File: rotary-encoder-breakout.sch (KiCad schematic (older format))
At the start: 3 parts, among them P4 CONN_01X02, P5 CONN_01X03

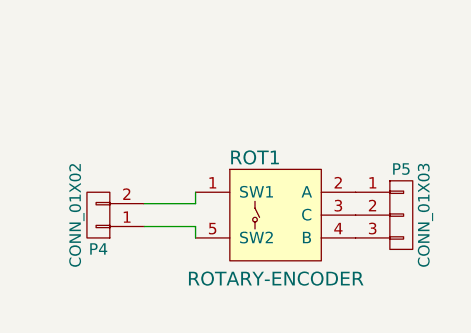
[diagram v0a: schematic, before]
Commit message: create version with pull-up resistors
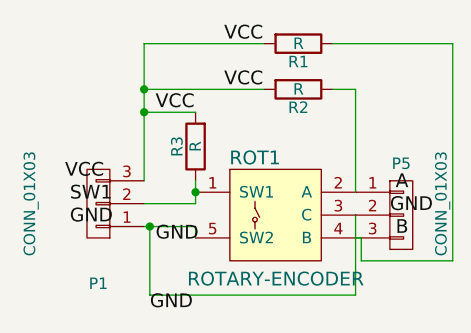
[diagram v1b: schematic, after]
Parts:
- removed P4: CONN_01X02, Pin_Headers:Pin_Header_Straight_1x02, symbol CONN_01X02
- added P1: CONN_01X03, Pin_Headers:Pin_Header_Straight_1x03, symbol CONN_01X03
- added R1, R2, R3: R, Resistors_SMD:R_1206, symbol R
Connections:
- net at P5.1 (P1), ROT1.2 (A): now also R2.1
- net at P5.2 (P2), ROT1.3 (C): now also ROT1.5 (SW2), P1.1 (P1)
- net at P5.3 (P3), ROT1.4 (B): now also R1.1
- net at ROT1.1 (SW1): now also P1.2 (P2), R3.1
- new net VCC: P1.3 (P3), R1.2, R2.2, R3.2
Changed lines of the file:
@@
 LIBS:Symbols_Transformer-Diskrete_RevA
 LIBS:sparkfun
+LIBS:rotary-encoder-breakout-cache
 EELAYER 25 0
 EELAYER END
@@
 U 1 1 587E787E
 P 3075 2225
-F 0 "P5" H 3075 2425 50  0000 C CNN
-F 1 "CONN_01X03" V 3175 2225 50  0000 C CNN
+F 0 "P5" H 3075 2450 50  0000 C CNN
+F 1 "CONN_01X03" V 3250 2275 50  0000 C CNN
 F 2 "Pin_Headers:Pin_Header_Straight_1x03" H 3075 2225 50  0001 C CNN
 F 3 "" H 3075 2225 50  0000 C CNN
@@
 	1    0    0    -1
 $EndComp
-$Comp
-L CONN_01X02 P4
-U 1 1 587E7945
-P 1750 2225
-F 0 "P4" H 1750 2375 50  0000 C CNN
-F 1 "CONN_01X02" V 1850 2225 50  0000 C CNN
-F 2 "Pin_Headers:Pin_Header_Straight_1x02" H 1750 2225 50  0001 C CNN
-F 3 "" H 1750 2225 50  0000 C CNN
-	1    1750 2225
-	-1   0    0    1
-$EndComp
-Wire Wire Line
-	1950 2175 2175 2175
-Wire Wire Line
-	2175 2175 2175 2125
-Wire Wire Line
-	1950 2275 2175 2275
-Wire Wire Line
-	2175 2275 2175 2325
 $Comp
 L ROTARY-ENCODER ROT1
@@
 	1    0    0    -1
 $EndComp
+$Comp
+L R R1
+U 1 1 58C20278
+P 2625 1475
+F 0 "R1" V 2705 1475 50  0000 C CNN
+F 1 "R" V 2625 1475 50  0000 C CNN
+F 2 "Resistors_SMD:R_1206" V 2555 1475 50  0001 C CNN
+F 3 "" H 2625 1475 50  0000 C CNN
+	1    2625 1475
+	0    1    1    0
+$EndComp
+$Comp
+L R R2
+U 1 1 58C203BF
+P 2625 1675
+F 0 "R2" V 2705 1675 50  0000 C CNN
+F 1 "R" V 2625 1675 50  0000 C CNN
+F 2 "Resistors_SMD:R_1206" V 2555 1675 50  0001 C CNN
+F 3 "" H 2625 1675 50  0000 C CNN
+	1    2625 1675
+	0    1    1    0
+$EndComp
+$Comp
+L CONN_01X03 P1
+U 1 1 58C20594
+P 1750 2175
+F 0 "P1" H 1750 2525 50  0000 C CNN
+F 1 "CONN_01X03" V 2050 2175 50  0000 C CNN
+F 2 "Pin_Headers:Pin_Header_Straight_1x03" H 1750 2175 50  0001 C CNN
+F 3 "" H 1750 2175 50  0000 C CNN
+	1    1750 2175
+	-1   0    0    1
+$EndComp
+Wire Wire Line
+	2175 2175 1950 2175
+Wire Wire Line
+	2175 2075 2175 2175
+Wire Wire Line
+	1950 2275 2175 2275
+Wire Wire Line
+	2175 2275 2175 2325
+Wire Wire Line
+	2875 1675 2875 2125
+Wire Wire Line
+	2875 2325 2900 2325
+Wire Wire Line
+	2900 2325 2900 2425
+Wire Wire Line
+	2900 2425 3300 2425
+Wire Wire Line
+	3300 2425 3300 1475
+Wire Wire Line
+	1950 1475 1950 2075
+Connection ~ 2175 2125
+$Comp
+L R R3
+U 1 1 58C207B9
+P 2175 1925
+F 0 "R3" V 2255 1925 50  0000 C CNN
+F 1 "R" V 2175 1925 50  0000 C CNN
+F 2 "Resistors_SMD:R_1206" V 2105 1925 50  0001 C CNN
+F 3 "" H 2175 1925 50  0000 C CNN
+	1    2175 1925
+	-1   0    0    1
+$EndComp
+Wire Wire Line
+	1950 1475 2475 1475
+Wire Wire Line
+	2475 1675 1950 1675
+Connection ~ 1950 1675
+Wire Wire Line
+	2175 1775 1950 1775
+Connection ~ 1950 1775
+Wire Wire Line
+	2775 1675 2875 1675
+Wire Wire Line
+	3300 1475 2775 1475
+Wire Wire Line
+	2875 2225 2875 2575
+Wire Wire Line
+	2875 2575 1975 2575
+Wire Wire Line
+	1975 2575 1975 2275
+Connection ~ 1975 2275
+Text Label 1975 2650 0    60   ~ 0
+GND
+Text Label 2000 2350 0    60   ~ 0
+GND
+Text Label 3025 2225 0    60   ~ 0
+GND
+Text Label 3050 2125 0    60   ~ 0
+A
+Text Label 3050 2325 0    60   ~ 0
+B
+Text Label 2300 1475 0    60   ~ 0
+VCC
+Text Label 2300 1675 0    60   ~ 0
+VCC
+Text Label 1775 2075 2    60   ~ 0
+VCC
+Text Label 2000 1775 0    60   ~ 0
+VCC
+Text Label 1625 2175 0    60   ~ 0
+SW1
+Text Label 1625 2275 0    60   ~ 0
+GND
 $EndSCHEMATC
